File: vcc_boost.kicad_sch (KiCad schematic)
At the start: 31 parts, among them Q1201 SQJ974EP, U1201 LM5122MHX/NOPB, U1202 DAC

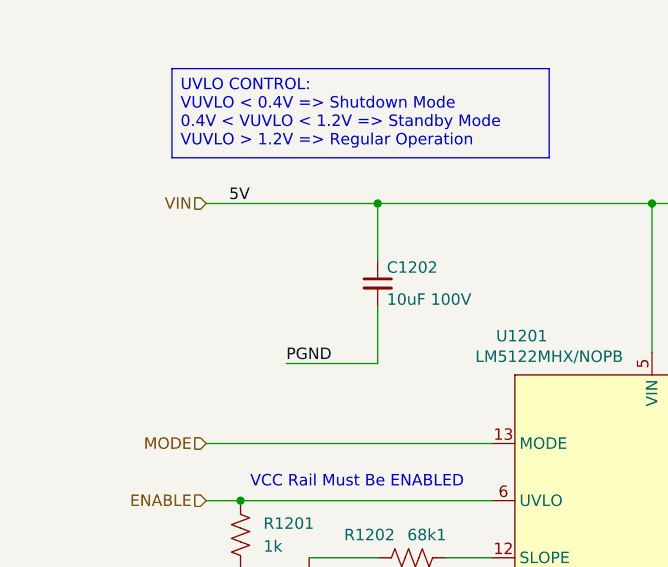
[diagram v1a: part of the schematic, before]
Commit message: switching dcdc
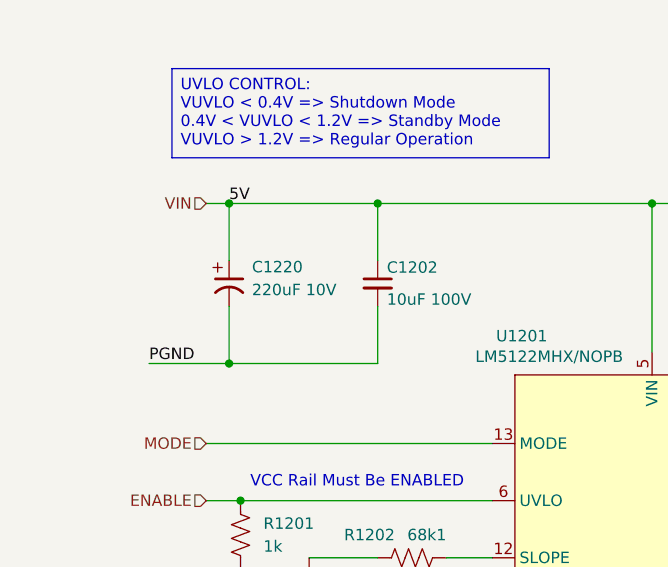
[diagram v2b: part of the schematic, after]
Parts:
- added C1220: 220uF 10V, BR_Passives:CAP-Electrolytic_SMD_D6.3-L6.6-W6.6-LS7.4-FD, symbol BR_Capacitors_Electrolytic:C_Alum_220uF_10V_20%_SMD
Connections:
- net PGND: now also C1220.2 (-)
- net VIN: now also C1220.1 (+)
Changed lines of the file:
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@@
 	)
 	(junction
+		(at 48.26 100.33)
+		(diameter 0)
+		(color 0 0 0 0)
+	)
+	(junction
 		(at 68.58 196.85)
 		(diameter 0)
@@
 	)
 	(junction
+		(at 48.26 118.11)
+		(diameter 0)
+		(color 0 0 0 0)
+	)
+	(junction
 		(at 368.3 144.78)
 		(diameter 0)
@@
 	(wire
 		(pts
-			(xy 260.35 127) (xy 275.59 127)
+			(xy 48.26 118.11) (xy 64.77 118.11)
 		)
 		(stroke
@@
 	(wire
 		(pts
-			(xy 64.77 111.76) (xy 64.77 118.11)
+			(xy 260.35 127) (xy 275.59 127)
 		)
 		(stroke
@@
 	(wire
 		(pts
+			(xy 64.77 118.11) (xy 64.77 111.76)
+		)
+		(stroke
+			(width 0)
+			(type default)
+		)
+	)
+	(wire
+		(pts
 			(xy 275.59 118.11) (xy 275.59 127)
 		)
@@
 	(wire
 		(pts
+			(xy 48.26 111.76) (xy 48.26 118.11)
+		)
+		(stroke
+			(width 0)
+			(type default)
+		)
+	)
+	(wire
+		(pts
 			(xy 171.45 139.7) (xy 171.45 142.24)
 		)
@@
 	(wire
 		(pts
-			(xy 45.72 100.33) (xy 64.77 100.33)
+			(xy 45.72 100.33) (xy 48.26 100.33)
 		)
 		(stroke
@@
 	(wire
 		(pts
-			(xy 64.77 118.11) (xy 54.61 118.11)
+			(xy 39.37 118.11) (xy 48.26 118.11)
 		)
 		(stroke
@@
 	(wire
 		(pts
+			(xy 48.26 100.33) (xy 64.77 100.33)
+		)
+		(stroke
+			(width 0)
+			(type default)
+		)
+	)
+	(wire
+		(pts
 			(xy 57.15 146.05) (xy 66.04 146.05)
 		)
@@
 	(wire
 		(pts
+			(xy 48.26 100.33) (xy 48.26 106.68)
+		)
+		(stroke
+			(width 0)
+			(type default)
+		)
+	)
+	(wire
+		(pts
 			(xy 275.59 100.33) (xy 290.83 100.33)
 		)
@@
 	)
 	(label "PGND"
-		(at 54.61 118.11 0)
+		(at 39.37 118.11 0)
 		(effects
 			(font
@@
 					(unit 1)
 				)
+			)
+		)
+	)
+	(symbol
+		(lib_id "BR_Capacitors_Electrolytic:C_Alum_220uF_10V_20%_SMD")
+		(at 48.26 109.22 0)
+		(unit 1)
+		(body_style 1)
+		(exclude_from_sim no)
+		(in_bom yes)
+		(on_board yes)
+		(in_pos_files yes)
+		(dnp no)
+		(fields_autoplaced yes)
+		(property "Reference" "C1220"
+			(at 50.8 107.3901 0)
+			(show_name no)
+			(do_not_autoplace no)
+			(effects
+				(font
+					(size 1.27 1.27)
+				)
+				(justify left)
+			)
+		)
+		(property "Value" "220uF 10V"
+			(at 50.8 109.9301 0)
+			(show_name no)
+			(do_not_autoplace no)
+			(effects
+				(font
+					(size 1.27 1.27)
+				)
+				(justify left)
+			)
+		)
+		(property "Footprint" "BR_Passives:CAP-Electrolytic_SMD_D6.3-L6.6-W6.6-LS7.4-FD"
+			(at 48.26 33.02 0)
+			(hide yes)
+			(show_name no)
+			(do_not_autoplace no)
+			(effects
+				(font
+					(size 1.27 1.27)
+				)
+				(justify left)
+			)
+		)
+		(property "Datasheet" "https://www.lcsc.com/datasheet/C72495.pdf"
+			(at 48.26 35.56 0)
+			(hide yes)
+			(show_name no)
+			(do_not_autoplace no)
+			(effects
+				(font
+					(size 1.27 1.27)
+				)
+				(justify left)
+			)
+		)
+		(property "Description" "220uF 10V 20% Electrolytic Capacitor SMD D6.3xL7.7mm"
+			(at 48.26 38.1 0)
+			(hide yes)
+			(show_name no)
+			(do_not_autoplace no)
+			(effects
+				(font
+					(size 1.27 1.27)
+				)
+				(justify left)
+			)
+		)
+		(property "Manufacturer" "ROQANG"
+			(at 48.26 40.64 0)
+			(hide yes)
+			(show_name no)
+			(do_not_autoplace no)
+			(effects
+				(font
+					(size 1.27 1.27)
+				)
+				(justify left)
+			)
+		)
+		(property "Manufacturer Part Num" "RVT1A221M0607"
+			(at 48.26 43.18 0)
+			(hide yes)
+			(show_name no)
+			(do_not_autoplace no)
+			(effects
+				(font
+					(size 1.27 1.27)
+				)
+				(justify left)
+			)
+		)
+		(property "BRE Number" "BRE-001440"
+			(at 48.26 45.72 0)
+			(hide yes)
+			(show_name no)
+			(do_not_autoplace no)
+			(effects
+				(font
+					(size 1.27 1.27)
+				)
+				(justify left)
+			)
+		)
+		(property "Supplier 1" "JLCPCB"
+			(at 48.26 48.26 0)
+			(hide yes)
+			(show_name no)
+			(do_not_autoplace no)
+			(effects
+				(font
+					(size 1.27 1.27)
+				)
+				(justify left)
+			)
+		)
+		(property "Supplier 1 Part Num" "C72495"
+			(at 48.26 50.8 0)
+			(hide yes)
+			(show_name no)
+			(do_not_autoplace no)
+			(effects
+				(font
+					(size 1.27 1.27)
+				)
+				(justify left)
+			)
+		)
+		(property "JLCPCB Part Num" "C72495"
+			(at 48.26 53.34 0)
+			(hide yes)
+			(show_name no)
+			(do_not_autoplace no)
+			(effects
+				(font
+					(size 1.27 1.27)
+				)
+				(justify left)
+			)
+		)
+		(pin "1"
+		)
+		(pin "2"
+		)
+		(instances
+			(project "PingDevKit"
+				(path "/2a5ce3ef-537a-4122-a1be-ef76186bc0d7/774f2c6c-c15c-4713-acf0-4edb2ec6be20/f57da81d-26f9-4e44-8192-6054ea342dd6"
+					(reference "C1220")
+					(unit 1)
+				)

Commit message: more work
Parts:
- C1204: symbol BR_Capacitors_0201:C_0201_100nF_25V_X7R_10% -> BR_Capacitors_0201:C_0201_100nF_25V_X5R_10%
- C1220: value 220uF 10V -> 220uF 50V
- NT1201: value Net_Tie_0201 -> Net Tie
- R1205: Supplier 1 DigiKey -> (none); Supplier 2 Mouser -> (none); Supplier 3 JLCPCB -> (none); Supplier Part Num 1 13-PE0805FRE470R009ZCT-ND -> (none); Supplier Part Num 2 603-P0805FRE470R009Z -> (none); Supplier Part Num 3 C6142798 -> (none)
- TP1201: value VTX -> TP_RING_TH
- TP1202: value GND -> TP_RING_TH
- U1202: value DAC -> DAC53401DSGR
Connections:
- net I2C4.SCL renamed I2C.SCL
- net I2C4.SDA renamed I2C.SDA
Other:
- note added: "5V Input"
- moved on the sheet: C1201, C1202, C1203, C1204, C1205, C1206, C1207, C1209, C1210, C1211, C1212, C1213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

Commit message: more work
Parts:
- added C1215: 220uF 50V, BR_Passives:CAP-Electrolytic_SMD_D6.3-L6.6-W6.6-LS7.4-FD, symbol BR_Capacitors_Electrolytic:C_Alum_220uF_10V_20%_SMD
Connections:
- net PGND: now also C1215.2 (-)
- net VIN: now also C1215.1 (+)

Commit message: more work
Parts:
- removed C1201: 10nF 50V, BR_Passives:C_0402_1005Metric-minimized, symbol BR_Capacitors_0402:C_0402_10nF_50V_X7R_10%
- removed C1202, C1211, C1212: 10uF 100V, BR_Passives:C_1210_3225Metric, symbol BR_Capacitors_1210:C_1210_10uF_100V_X7S_10%
- removed C1203: 470nF 16V, BR_Passives:C_0402_1005Metric-minimized, symbol BR_Capacitors_0402:C_0402_470nF_16V_X7R_10%
- removed C1204: 100nF 25V, BR_Passives:C_0201_0603Metric-minimized, symbol BR_Capacitors_0201:C_0201_100nF_25V_X5R_10%
- removed C1205: 22nF 50V, BR_Passives:C_0402_1005Metric, symbol BR_Capacitors_0402:C_0402_22nF_50V_X7R_10%
- removed C1206: 1uF 50V, BR_Passives:C_0402_1005Metric-minimized, symbol BR_Capacitors_0402:C_0402_1uF_50V_X5R_10%
- removed C1207: 10uF 16V, BR_Passives:C_0603_1608Metric-minimized, symbol BR_Capacitors_0603:C_0603_10uF_16V_X5R_10%_AEC-Q200
- removed C1209, C1210: 100nF 100V, BR_Passives:C_0603_1608Metric-minimized, symbol BR_Capacitors_0603:C_0603_100nF_100V_X7R_AEC-Q200
- removed C1215, C1220: 220uF 50V, BR_Passives:CAP-Electrolytic_SMD_D6.3-L6.6-W6.6-LS7.4-FD, symbol BR_Capacitors_Electrolytic:C_Alum_220uF_10V_20%_SMD
- removed D1201: BAS20H, BR_Discretes:D_SOD-323, symbol BR_Diodes:D_BAS20H
- removed L1201: 10uH 30A, BR_Inductors:FC-SE2918-100M-28A, symbol BR_Inductors:L_FC-SE2918-100M-28A
- removed NT1: Net_Tie_0603, BR_Virtual_Parts:Net_Tie_0603_1608Metric, symbol BR_Virtual_Parts:Net_Tie_0603
- removed NT1201: Net Tie, BR_Virtual_Parts:NetTie-2_SMD_Pad_3.88mm_wide, symbol BR_Virtual_Parts:NetTie-2_3.88mm
- removed Q1201: SQJ974EP, BR_SOP:PowerPAK_SO-8_Dual, symbol BR_Transistors:MFET_N_ARRAY_SQJ974EP
- removed R1202: 68k1, BR_Passives:C_0402_1005Metric-minimized, symbol BR_Resistors_0402:R_0402_68k1
- removed R1203: 2k2, BR_Passives:R_0402_1005Metric-minimized, symbol BR_Resistors_0402:R_0402_2k2
- removed R1204: 75k, BR_Passives:R_0402_1005Metric-minimized, symbol BR_Resistors_0402:R_0402_75k
- removed R1205: 3mR, BR_Passives:R_2512_6332Metric, symbol BR_Resistors_2512:R_2512_3mR
- removed R1206: 137k, BR_Passives:C_0402_1005Metric-minimized, symbol BR_Resistors_0402:R_0402_137k
- removed R1207: 10k, BR_Passives:C_0402_1005Metric-minimized, symbol BR_Resistors_0402:R_0402_10k
- removed R1208: 24k9, BR_Passives:C_0402_1005Metric-minimized, symbol BR_Resistors_0402:R_0402_24k9
- removed U1201: LM5122MHX/NOPB, BR_SOP:HTSSOP-20-1EP_4.4x6.5mm_P0.65mm_EP2.85x4mm, symbol BR_IC_Regulators:LM5122MHX/NOPB
- added C1201, C1205: 10uF 100V, BR_Passives:C_1210_3225Metric, symbol BR_Capacitors_1210:C_1210_10uF_100V_X7S_10%
- added C1202: 2n2F 50V, BR_Passives:C_0201_0603Metric-minimized, symbol BR_Capacitors_0201:C_0201_2n2F_50V_X7R_10%
- added C1203: 1uF 16V, BR_Passives:C_0201_0603Metric-minimized, symbol BR_Capacitors_0201:C_0201_1uF_16V_X5R_10%
- added C1204: 10nF 35V, BR_Passives:C_0402_1005Metric-minimized, symbol BR_Capacitors_0402:C_0402_10nF_35V_C0G_2%
- added D1201: 60V 3A, BR_Discretes:SMA_L4.4-W2.6-LS5.0-RD, symbol BR_Diodes:B360A-13-F
- added L1201: 10uH 8A, BR_Inductors:SRP7050WA, symbol BR_Inductors:L_SRP7050WA-100M
- added NT1202: NetTie-2_0.18mm, BR_Virtual_Parts:NetTie-2_SMD_Pad_1.7mm_wide, symbol BR_Virtual_Parts:NetTie-2_1.7mm_wide
- added R1201: 36k5, BR_Passives:C_0402_1005Metric-minimized, symbol BR_Resistors_0402:R_0402_36k5
- added R1202: 63.4k, BR_Passives:C_0402_1005Metric-minimized, symbol BR_Resistors_0402:R_0402_63.4k
- added R1203: 100k, BR_Passives:C_0402_1005Metric-minimized, symbol BR_Resistors_0402:R_0402_100k
- added R1204: 9k65, BR_Passives:C_0402_1005Metric-minimized, symbol BR_Resistors_0402:R_0402_9k65
- added R1205: 13.3k, BR_Passives:C_0402_1005Metric-minimized, symbol BR_Resistors_0402:R_0402_13k3
- added R1206: 0R, BR_Passives:R_0402_1005Metric, symbol BR_Resistors_0402:R_0402_0R
- added U1201: LT8364, BR_IC:DFN-12_L4.0-W3.0-P0.50-BL-EP, symbol BR_PMIC:LT8364EDE#TRPBF
- renumbered R1201 to R2001, TP1202 to TP2001, TP1201 to TP2002
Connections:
- net ENABLE: now also U1201.2 (EN/UVLO)
- net GND: now also C1202.2, C1203.1, C1204.2, NT1202.2, R1202.2, R1204.2, R1206.1, U1201.5 (BIAS)
- net PGND: now also C1201.2, C1205.2, NT1202.1, U1201.13 (GND)
- net VIN: now also C1201.1, L1201.1, U1201.3 (VIN)
- net VTX: now also C1205.1, D1201.1 (K), R1203.1
- net VDAC: now reaches R1.1, U1202.8 (OUT)
- net VDAC: now also R1205.1
- new net: R1202.1, U1201.8 (RT)
- new net: R1203.2, R1204.1, R1205.2, U1201.7 (FBX)
- new net: C1202.1, R1201.2
- new net: R1201.1, U1201.6 (VC)
- new net: D1201.2 (A), L1201.2, U1201.11 (SW2), U1201.12 (SW1)
- new net: R1206.2, U1201.10 (SYNC/MODE)
- new net: C1203.2, U1201.4 (INTVCC)
- new net: C1204.1, U1201.9 (SS)
- no-connect marks 1 -> 0
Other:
- note removed: "RESISTORS FOR 10V-24V X: RDAC Y: RFBT"
- note removed: "RESISTORS FOR 10V-36V X: RDAC Y: RFBT"
- note removed: "RESISTORS FOR 10V-48V X: RDAC Y: RFBT"
- note removed: "RESISTORS FOR 6V-24V X: RDAC Y: RFBT"
- note removed: "VCC Rail Must Be ENABLED"
- moved on the sheet: R2001, TP2001, TP2002

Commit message: more work
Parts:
- renumbered C1214 to C1202, C1213 to C1203, C1202 to C1205, C1203 to C1206, C1205 to C1207, NT1202 to NT1201, R2001 to R1201, R1206 to R1202, R1202 to R1203, R1 to R1204, R1201 to R1205, R1205 to R1206, R1203 to R1207, R1204 to R1208, TP2001 to TP1201, TP2002 to TP1202, U1202 to U1201, U1201 to U1202

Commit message: more work
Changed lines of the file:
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@@
-	)
-	(junction
-		(at 151.13 228.6)
-		(diameter 0)
-		(color 0 0 0 0)
 	)
 	(junction
@@
 		)
 	)
+	(label "VDAC"
+		(at 151.13 228.6 0)
+		(effects
+			(font
+				(size 1.27 1.27)
+			)
+			(justify left bottom)
+		)
+	)
 	(label "I2C.SCL"
 		(at 104.14 229.87 0)
@@
 	(label "I2C.SDA"
 		(at 104.14 232.41 0)
+		(effects
+			(font
+				(size 1.27 1.27)
+			)
+			(justify left bottom)
+		)
+	)
+	(label "VDAC"
+		(at 177.8 127 0)
 		(effects
 			(font
@@
 	)
 	(symbol
-		(lib_id "BR_Virtual_Parts:VCC_LOCAL")
-		(at 151.13 228.6 0)
-		(unit 1)
-		(body_style 1)
-		(exclude_from_sim no)
-		(in_bom no)
-		(on_board yes)
-		(in_pos_files yes)
-		(dnp no)
-		(property "Reference" "#PWR01218"
-			(at 151.13 232.41 0)
-			(hide yes)
-			(show_name no)
-			(do_not_autoplace no)
-			(effects
-				(font
-					(size 1.27 1.27)
-				)
-			)
-		)
-		(property "Value" "VDAC"
-			(at 151.13 225.044 0)
-			(show_name no)
-			(do_not_autoplace no)
-			(effects
-				(font
-					(size 1.27 1.27)
-				)
-			)
-		)
-		(property "Footprint" ""
-			(at 151.13 228.6 0)
-			(hide yes)
-			(show_name no)
-			(do_not_autoplace no)
-			(effects
-				(font
-					(size 1.27 1.27)
-				)
-			)
-		)
-		(property "Datasheet" ""
-			(at 151.13 228.6 0)
-			(hide yes)
-			(show_name no)
-			(do_not_autoplace no)
-			(effects
-				(font
-					(size 1.27 1.27)
-				)
-			)
-		)
-		(property "Description" "Power symbol creates a local label with name \"VCC\" (Only visible for current sheet)"
-			(at 151.13 228.6 0)
-			(hide yes)
-			(show_name no)
-			(do_not_autoplace no)
-			(effects
-				(font
-					(size 1.27 1.27)
-				)
-			)
-		)
-		(pin "1"
-		)
-		(instances
-			(project "PingDevKit"
-				(path "/2a5ce3ef-537a-4122-a1be-ef76186bc0d7/774f2c6c-c15c-4713-acf0-4edb2ec6be20/f57da81d-26f9-4e44-8192-6054ea342dd6"
-					(reference "#PWR01218")
-					(unit 1)
-				)
-			)
-		)
-	)
-	(symbol
 		(lib_id "BR_Virtual_Parts:GND_ALT_LOCAL")
 		(at 107.95 95.25 0)
@@
 					(unit 1)
 				)
-			)
-		)
-	)
-	(symbol
-		(lib_id "BR_Virtual_Parts:VCC_LOCAL")
-		(at 177.8 127 0)
-		(unit 1)
-		(body_style 1)
-		(exclude_from_sim no)
-		(in_bom no)
-		(on_board yes)
-		(in_pos_files yes)
-		(dnp no)
-		(property "Reference" "#PWR01222"
-			(at 177.8 130.81 0)
-			(hide yes)
-			(show_name no)
-			(do_not_autoplace no)
-			(effects
-				(font
-					(size 1.27 1.27)
-				)
-			)
-		)
-		(property "Value" "VDAC"
-			(at 177.8 123.444 0)
-			(show_name no)
-			(do_not_autoplace no)
-			(effects
-				(font
-					(size 1.27 1.27)
-				)
-			)
-		)
-		(property "Footprint" ""
-			(at 177.8 127 0)
-			(hide yes)
-			(show_name no)
-			(do_not_autoplace no)
-			(effects
-				(font
-					(size 1.27 1.27)
-				)
-			)
-		)
-		(property "Datasheet" ""
-			(at 177.8 127 0)
-			(hide yes)
-			(show_name no)
-			(do_not_autoplace no)
-			(effects
-				(font
-					(size 1.27 1.27)
-				)
-			)
-		)
-		(property "Description" "Power symbol creates a local label with name \"VCC\" (Only visible for current sheet)"
-			(at 177.8 127 0)
-			(hide yes)
-			(show_name no)
-			(do_not_autoplace no)
-			(effects
-				(font
-					(size 1.27 1.27)
-				)
-			)
-		)
-		(pin "1"
-		)
-		(instances
-			(project "PingDevKit"
-				(path "/2a5ce3ef-537a-4122-a1be-ef76186bc0d7/774f2c6c-c15c-4713-acf0-4edb2ec6be20/f57da81d-26f9-4e44-8192-6054ea342dd6"
-					(reference "#PWR01222")
-					(unit 1)
-				)

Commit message: work
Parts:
- removed TP1201, TP1202: TP_RING_TH, BR_Connectors:TEST-TH_BD2.54-P1.4_RED, symbol BR_Connectors:TP_Ring_PTH
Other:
- moved on the sheet: C1201, C1202, C1203, C1204, C1205, C1206, C1207, D1201, L1201, NT1201, R1201, R1202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
